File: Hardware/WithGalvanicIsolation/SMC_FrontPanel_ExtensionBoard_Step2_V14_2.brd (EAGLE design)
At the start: 99.3 x 50.1 mm, 91 parts, among them J1 PIN2F061.060, J2 PIN2F061.060, J3 to mainboardconnector J3, J4 to Displaypanel, M1 ARDUINO-PRO-MINI-RAW, T1 BC857, T2 BC857, T3 BC857, T4 BC857, T5 BC857C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

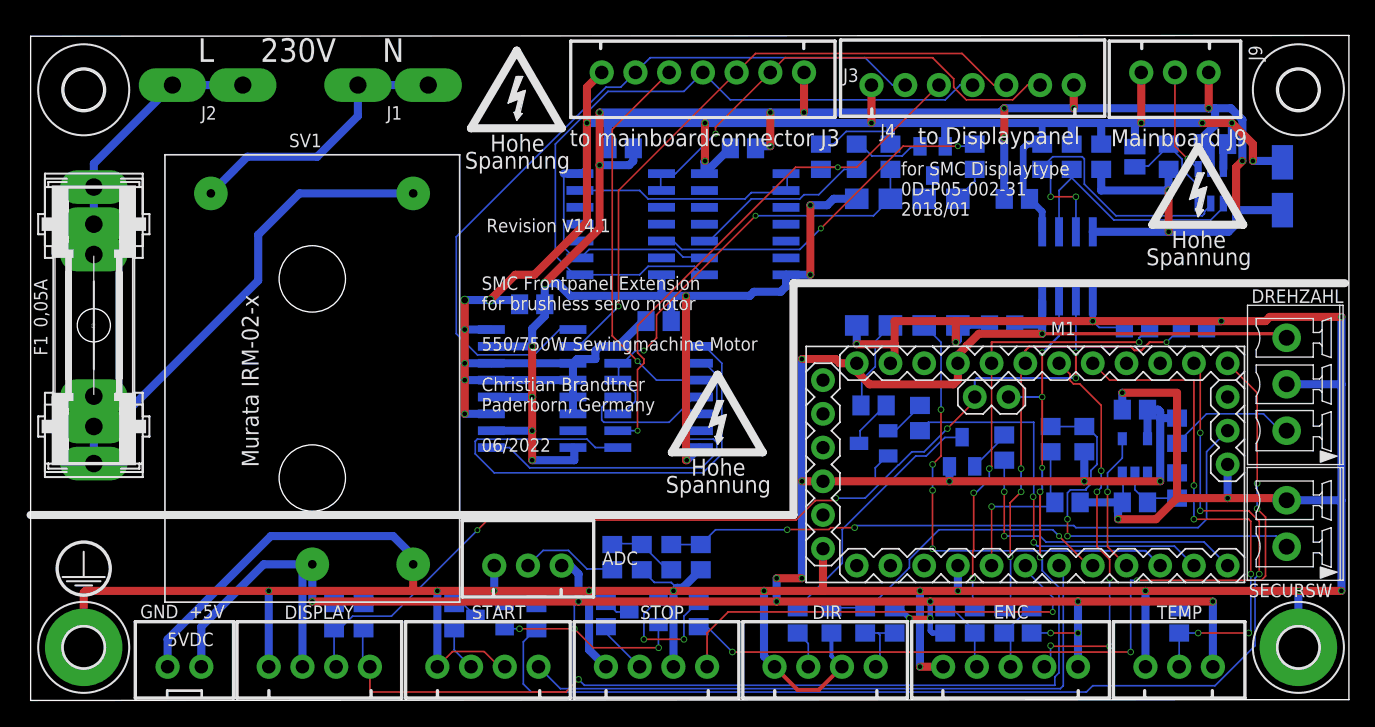
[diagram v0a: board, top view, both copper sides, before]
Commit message: Update Revision 14.2 J3 Ausrichtung getauscht um fertige Kabel verwenden zu können. Kosmetik
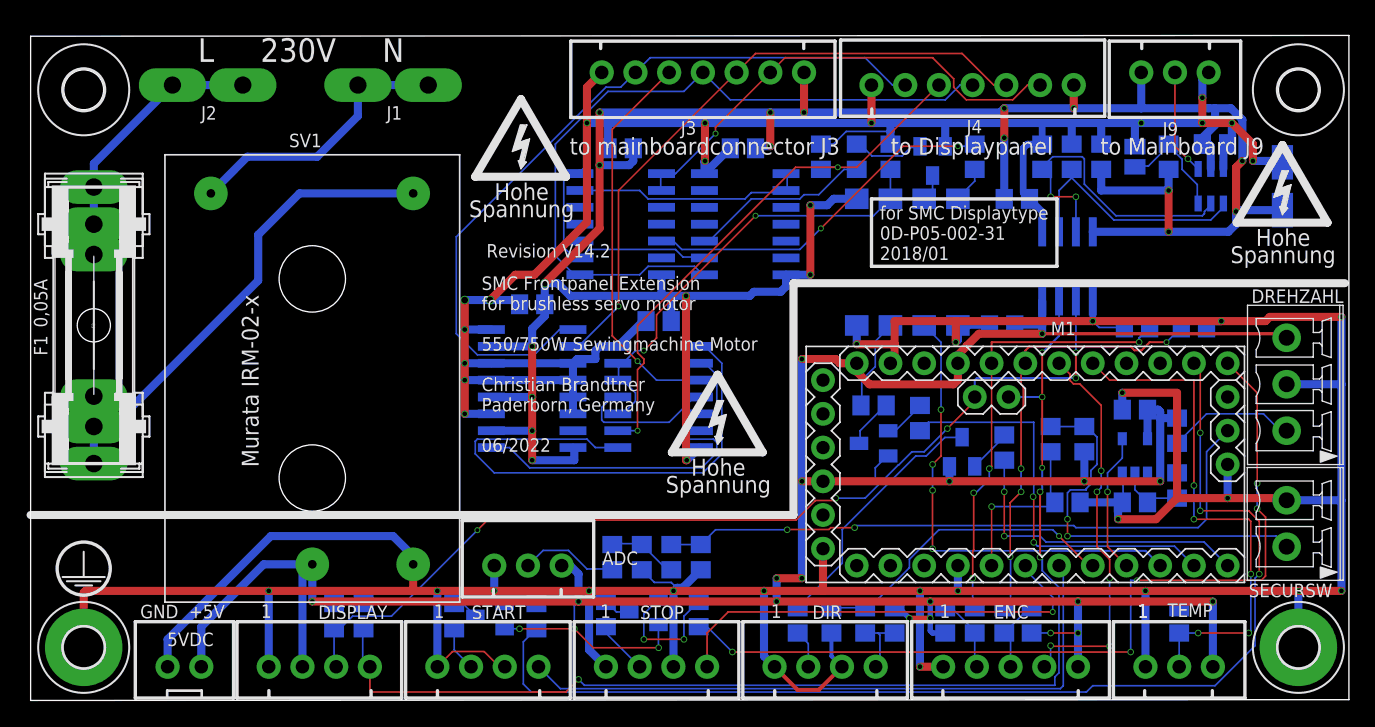
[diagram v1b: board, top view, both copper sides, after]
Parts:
- moved U$54 6.35 mm to (94.3, 38.9)
- moved U$57 3.67 mm to (36.9, 42.4)
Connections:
- net HGND: now also J9.3; no longer J9.1
- net HVCC: now also J9.1; no longer J9.3
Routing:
- net HGND: track 200.0 -> 199.6 mm, vias 22 -> 21
- net HVCC: track 185.2 -> 185.4 mm, vias 14 -> 15
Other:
- board text added: "ADC"
- board text added: "Revision V14.2"
- board text added: "to Mainboard J9"
- board text removed: "Mainboard J9"
- board text removed: "Revision V14.1"
